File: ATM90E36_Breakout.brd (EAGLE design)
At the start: 50 x 50 mm, 71 parts, among them IC1 ATM90E36, J1 GREEN-2P-3.5, J2 ST-PJ-312, J3 ST-PJ-312, J4 GREEN-2P-3.5, J5 ST-PJ-312, J6 ST-PJ-312, Q1 FA-128

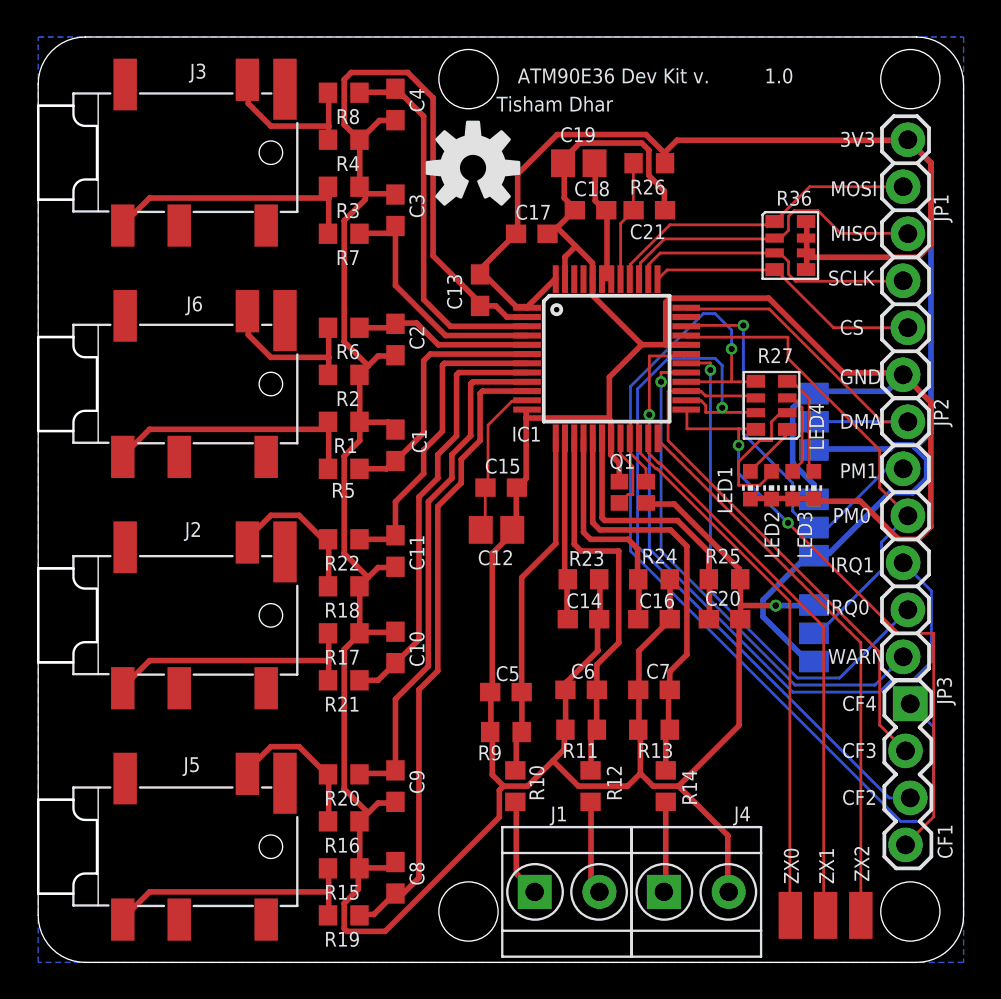
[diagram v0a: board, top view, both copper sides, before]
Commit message: Renamed CT's and improved cutouts
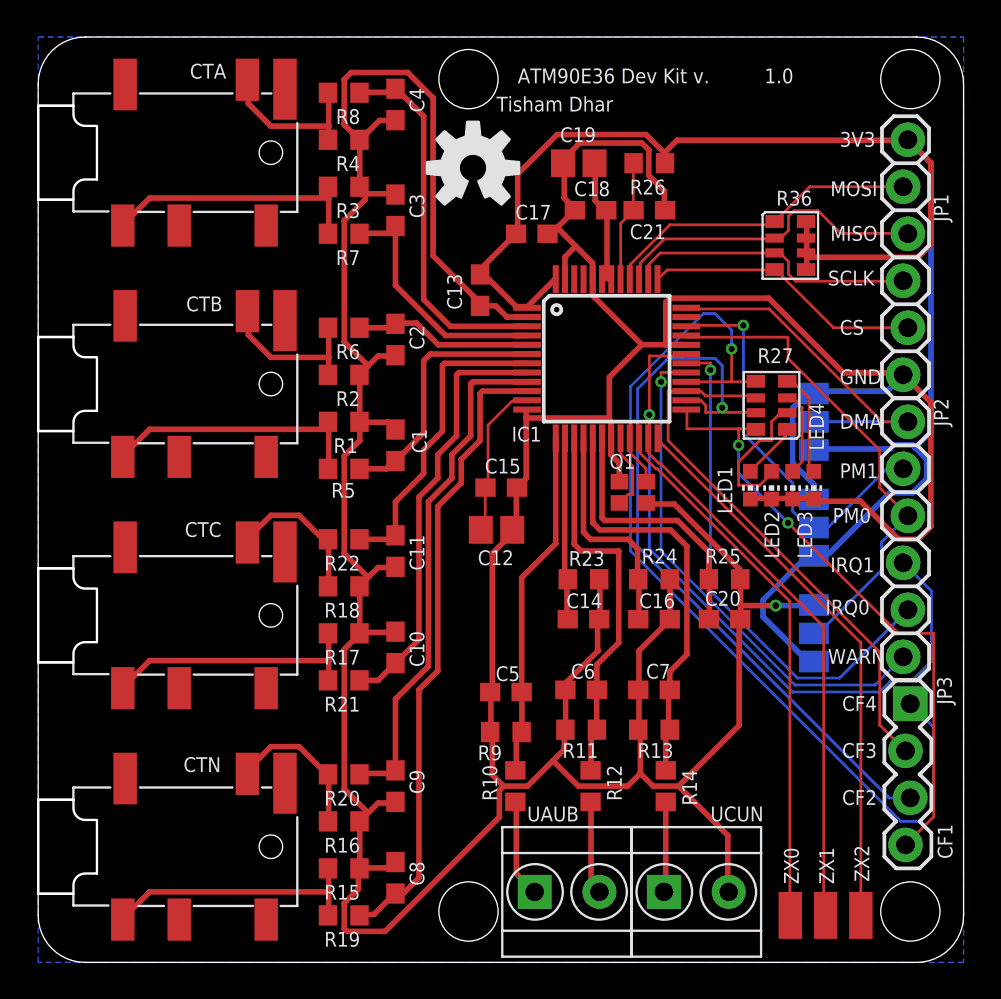
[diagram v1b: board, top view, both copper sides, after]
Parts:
- renumbered J1 to UAUB, J2 to CTC, J3 to CTA, J4 to UCUN, J5 to CTN, J6 to CTB
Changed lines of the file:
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@@
 <layer number="21" name="tPlace" color="7" fill="1" visible="yes" active="yes"/>
 <layer number="22" name="bPlace" color="7" fill="1" visible="yes" active="yes"/>
-<layer number="23" name="tOrigins" color="15" fill="1" visible="no" active="yes"/>
+<layer number="23" name="tOrigins" color="15" fill="1" visible="yes" active="yes"/>
 <layer number="24" name="bOrigins" color="15" fill="1" visible="no" active="yes"/>
 <layer number="25" name="tNames" color="7" fill="1" visible="yes" active="yes"/>
@@
 <layer number="44" name="Drills" color="7" fill="1" visible="no" active="yes"/>
 <layer number="45" name="Holes" color="7" fill="1" visible="no" active="yes"/>
-<layer number="46" name="Milling" color="3" fill="1" visible="no" active="yes"/>
+<layer number="46" name="Milling" color="3" fill="1" visible="yes" active="yes"/>
 <layer number="47" name="Measures" color="7" fill="1" visible="no" active="yes"/>
 <layer number="48" name="Document" color="7" fill="1" visible="no" active="yes"/>
@@
 </element>
 <element name="R10" library="adafruit" package="R0603" value="100K" x="25.781" y="9.525" smashed="yes" rot="R270">
-<attribute name="NAME" x="26.543" y="10.668" size="0.8" layer="25" font="vector" ratio="20" rot="R270"/>
+<attribute name="NAME" x="24.003" y="10.668" size="0.8" layer="25" font="vector" ratio="20" rot="R270"/>
 <attribute name="VALUE" x="23.749" y="10.414" size="0.8" layer="27" rot="R270"/>
 </element>
@@
 <attribute name="VALUE" x="31.877" y="10.414" size="0.8" layer="27" rot="R270"/>
 </element>
-<element name="J1" library="Seeed-Connector -2016" package="H2-3.5-7.0X7.0MM" value="GREEN-2P-3.5" x="28.575" y="3.81" smashed="yes">
-<attribute name="NAME" x="27.686" y="7.62" size="0.8" layer="25" font="vector" ratio="20"/>
+<element name="UAUB" library="Seeed-Connector -2016" package="H2-3.5-7.0X7.0MM" value="GREEN-2P-3.5" x="28.575" y="3.81" smashed="yes">
+<attribute name="NAME" x="26.416" y="7.62" size="0.8" layer="25" font="vector" ratio="20"/>
 <attribute name="VALUE" x="26.67" y="-0.635" size="0.8" layer="27" ratio="11"/>
 </element>
-<element name="J4" library="Seeed-Connector -2016" package="H2-3.5-7.0X7.0MM" value="GREEN-2P-3.5" x="35.56" y="3.81" smashed="yes">
-<attribute name="NAME" x="37.592" y="7.62" size="0.8" layer="25" font="vector" ratio="20"/>
+<element name="UCUN" library="Seeed-Connector -2016" package="H2-3.5-7.0X7.0MM" value="GREEN-2P-3.5" x="35.56" y="3.81" smashed="yes">
+<attribute name="NAME" x="36.322" y="7.62" size="0.8" layer="25" font="vector" ratio="20"/>
 <attribute name="VALUE" x="33.655" y="-0.635" size="0.8" layer="27" ratio="11"/>
 </element>
-<element name="J3" library="Seeed-Connector -2016" package="AUDIO6P-SMD-3.5-14.0X6.4X5.0MM" value="ST-PJ-312" x="0" y="43.75" smashed="yes" rot="R180">
+<element name="CTA" library="Seeed-Connector -2016" package="AUDIO6P-SMD-3.5-14.0X6.4X5.0MM" value="ST-PJ-312" x="0" y="43.75" smashed="yes" rot="R180">
 <attribute name="MPN" value="ST-PJ-312" x="0" y="43.75" size="1.778" layer="27" rot="R180" display="off"/>
 <attribute name="NAME" x="8.193" y="47.752" size="0.8" layer="25" font="vector" ratio="20"/>
 <attribute name="VALUE" x="10.16" y="48.195" size="0.8" layer="27" ratio="11" rot="R180"/>
 </element>
-<element name="J6" library="Seeed-Connector -2016" package="AUDIO6P-SMD-3.5-14.0X6.4X5.0MM" value="ST-PJ-312" x="0" y="31.25" smashed="yes" rot="R180">
+<element name="CTB" library="Seeed-Connector -2016" package="AUDIO6P-SMD-3.5-14.0X6.4X5.0MM" value="ST-PJ-312" x="0" y="31.25" smashed="yes" rot="R180">
 <attribute name="MPN" value="ST-PJ-312" x="0" y="31.25" size="1.778" layer="27" rot="R180" display="off"/>
 <attribute name="NAME" x="7.993" y="35.179" size="0.8" layer="25" font="vector" ratio="20"/>
 <attribute name="VALUE" x="10.16" y="35.695" size="0.8" layer="27" ratio="11" rot="R180"/>
 </element>
-<element name="J2" library="Seeed-Connector -2016" package="AUDIO6P-SMD-3.5-14.0X6.4X5.0MM" value="ST-PJ-312" x="0" y="18.75" smashed="yes" rot="R180">
+<element name="CTC" library="Seeed-Connector -2016" package="AUDIO6P-SMD-3.5-14.0X6.4X5.0MM" value="ST-PJ-312" x="0" y="18.75" smashed="yes" rot="R180">
 <attribute name="MPN" value="ST-PJ-312" x="0" y="18.75" size="1.778" layer="27" rot="R180" display="off"/>
 <attribute name="NAME" x="7.92" y="22.987" size="0.8" layer="25" font="vector" ratio="20"/>
 <attribute name="VALUE" x="10.16" y="23.195" size="0.8" layer="27" ratio="11" rot="R180"/>
 </element>
-<element name="J5" library="Seeed-Connector -2016" package="AUDIO6P-SMD-3.5-14.0X6.4X5.0MM" value="ST-PJ-312" x="0" y="6.25" smashed="yes" rot="R180">
+<element name="CTN" library="Seeed-Connector -2016" package="AUDIO6P-SMD-3.5-14.0X6.4X5.0MM" value="ST-PJ-312" x="0" y="6.25" smashed="yes" rot="R180">
 <attribute name="MPN" value="ST-PJ-312" x="0" y="6.25" size="1.778" layer="27" rot="R180" display="off"/>
 <attribute name="NAME" x="7.847" y="10.287" size="0.8" layer="25" font="vector" ratio="20"/>
@@
 <contactref element="R5" pad="1"/>
 <contactref element="R1" pad="2"/>
-<contactref element="J6" pad="COM1"/>
+<contactref element="CTB" pad="COM1"/>
 <wire x1="15.6972" y1="29.1846" x2="15.6972" y2="26.67" width="0.3048" layer="1"/>
 <wire x1="15.6972" y1="26.67" x2="15.66" y2="26.67" width="0.3048" layer="1"/>
@@
 <contactref element="R4" pad="2"/>
 <contactref element="R8" pad="1"/>
-<contactref element="J3" pad="L"/>
+<contactref element="CTA" pad="L"/>
 <wire x1="15.6972" y1="46.9392" x2="15.6972" y2="45.1866" width="0.3048" layer="1"/>
 <wire x1="15.6972" y1="45.1866" x2="15.6972" y2="44.5008" width="0.3048" layer="1"/>
@@
 <contactref element="R2" pad="2"/>
 <contactref element="R6" pad="1"/>
-<contactref element="J6" pad="L"/>
+<contactref element="CTB" pad="L"/>
 <wire x1="15.6972" y1="34.29" x2="15.6972" y2="32.6898" width="0.3048" layer="1"/>
 <wire x1="15.6972" y1="32.6898" x2="15.6972" y2="31.7754" width="0.3048" layer="1"/>
@@
 <contactref element="R18" pad="2"/>
 <contactref element="R22" pad="1"/>
-<contactref element="J2" pad="L"/>
+<contactref element="CTC" pad="L"/>
 <wire x1="15.6972" y1="22.86" x2="15.6972" y2="20.3454" width="0.3048" layer="1"/>
 <wire x1="15.6972" y1="20.3454" x2="15.66" y2="20.32" width="0.3048" layer="1"/>
@@
 <contactref element="R21" pad="1"/>
 <contactref element="R17" pad="2"/>
-<contactref element="J2" pad="COM1"/>
+<contactref element="CTC" pad="COM1"/>
 <wire x1="15.6972" y1="17.7546" x2="15.6972" y2="16.3068" width="0.3048" layer="1"/>
 <wire x1="15.6972" y1="16.3068" x2="15.6972" y2="15.24" width="0.3048" layer="1"/>
@@
 <contactref element="C5" pad="2"/>
 <contactref element="C7" pad="2"/>
-<contactref element="J4" pad="2"/>
+<contactref element="UCUN" pad="2"/>
 <contactref element="IC1" pad="2"/>
 <contactref element="C12" pad="2"/>
@@
 <contactref element="R16" pad="2"/>
 <contactref element="R20" pad="1"/>
-<contactref element="J5" pad="L"/>
+<contactref element="CTN" pad="L"/>
 <wire x1="15.6972" y1="10.1346" x2="15.6972" y2="7.62" width="0.3048" layer="1"/>
 <wire x1="15.6972" y1="7.62" x2="15.66" y2="7.62" width="0.3048" layer="1"/>
@@
 <contactref element="R19" pad="1"/>
 <contactref element="R15" pad="2"/>
-<contactref element="J5" pad="COM1"/>
+<contactref element="CTN" pad="COM1"/>
 <wire x1="15.6972" y1="5.0292" x2="15.6972" y2="3.81" width="0.3048" layer="1"/>
 <wire x1="15.6972" y1="3.81" x2="15.6972" y2="2.5908" width="0.3048" layer="1"/>
@@
 <contactref element="R7" pad="1"/>
 <contactref element="R3" pad="2"/>
-<contactref element="J3" pad="COM1"/>
+<contactref element="CTA" pad="COM1"/>
 <wire x1="15.6972" y1="41.91" x2="15.6972" y2="41.3004" width="0.3048" layer="1"/>
 <wire x1="15.6972" y1="41.3004" x2="15.6972" y2="39.3954" width="0.3048" layer="1"/>
@@
 <signal name="UA" class="2">
 <contactref element="R10" pad="2"/>
-<contactref element="J1" pad="1"/>
+<contactref element="UAUB" pad="1"/>
 <wire x1="25.8318" y1="4.8006" x2="25.8318" y2="8.6106" width="0.3048" layer="1"/>
 <wire x1="26.8224" y1="3.81" x2="25.8318" y2="4.8006" width="0.3048" layer="1"/>
@@
 <signal name="UB" class="2">
 <contactref element="R12" pad="2"/>
-<contactref element="J1" pad="2"/>
+<contactref element="UAUB" pad="2"/>
 <wire x1="29.8704" y1="4.191" x2="29.8704" y2="8.6106" width="0.3048" layer="1"/>
 <wire x1="30.2514" y1="3.81" x2="29.8704" y2="4.191" width="0.3048" layer="1"/>
@@
 <signal name="UC" class="2">
 <contactref element="R14" pad="2"/>
-<contactref element="J4" pad="1"/>
+<contactref element="UCUN" pad="1"/>
 <wire x1="33.909" y1="3.8862" x2="33.909" y2="8.675" width="0.3048" layer="1"/>
 <wire x1="33.8328" y1="3.81" x2="33.909" y2="3.8862" width="0.3048" layer="1"/>
